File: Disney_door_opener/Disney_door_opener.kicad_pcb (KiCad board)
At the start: 2 copper layers, 70 x 43 mm, 29 parts, among them J1 Screw_Terminal_01x02, J2 Conn_01x02, J3 Conn_01x02, J4 Conn_01x05, J5 Screw_Terminal_01x02, U1 LM2596S-5, U2 ESP32_DevKit_V1_DOIT, U3 MAX98357A

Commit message: Changed esp32 board with 2 pinheader connectors. Updated resistor values for proper operation.
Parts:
- removed U2: ESP32_DevKit_V1_DOIT, Disney_door_opener:esp32_devkit_v1_doit
- added J6: Conn_01x15, Connector_PinHeader_2.54mm:PinHeader_1x15_P2.54mm_Vertical, F.Cu at (151.8, 32.5)
- added J7: Conn_01x15, Connector_PinHeader_2.54mm:PinHeader_1x15_P2.54mm_Vertical, F.Cu at (151.8, 58.0)
- R1, R2, R3, R5: value 100K -> DNI
- R4: value n.c. -> 630K
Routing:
- net Net-(J7-Pad8): vias 0 -> 1
- net Net-(J7-Pad7): vias 0 -> 1
- net GND: vias 238 -> 234

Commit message: Corrected swapped pins.
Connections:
- net Net-(J4-Pad3) renamed /CLK
- J4 pad 1: Net-(J4-Pad1) -> /LIGHT
- J4 pad 2: Net-(J4-Pad2) -> /CS
- J4 pad 4: Net-(J4-Pad4) -> /MISO
- J4 pad 5: Net-(J4-Pad5) -> /MOSI
- J6 pad 1: Net-(J4-Pad1) -> /MOSI
- J6 pad 10: Net-(J4-Pad4) -> Net-(J6-Pad10)
- J6 pad 6: Net-(J4-Pad2) -> /MISO
- J6 pad 8: Net-(J6-Pad8) -> /CS
- J7 pad 13: Net-(J4-Pad5) -> /LIGHT
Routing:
- net /MOSI: track 0.00 -> 57.6 mm, vias 0 -> 1
- net Net-(J4-Pad1): track 55.0 -> 0.00 mm
- net Net-(J4-Pad5): track 45.7 -> 0.00 mm
- net /MISO: track 0.00 -> 45.7 mm, vias 0 -> 2
- net Net-(J4-Pad2): track 40.3 -> 0.00 mm
- net /LIGHT: track 0.00 -> 34.7 mm
- net /CS: track 0.00 -> 32.8 mm
- net Net-(J4-Pad4): track 24.9 -> 0.00 mm
- net /CLK: track 37.2 -> 31.5 mm
- net GND: track 42.0 -> 46.7 mm, vias 234 -> 235
- net Net-(J7-Pad8): vias 1 -> 0
- net Net-(J7-Pad7): vias 1 -> 0
- net (no net): vias 3 -> 0

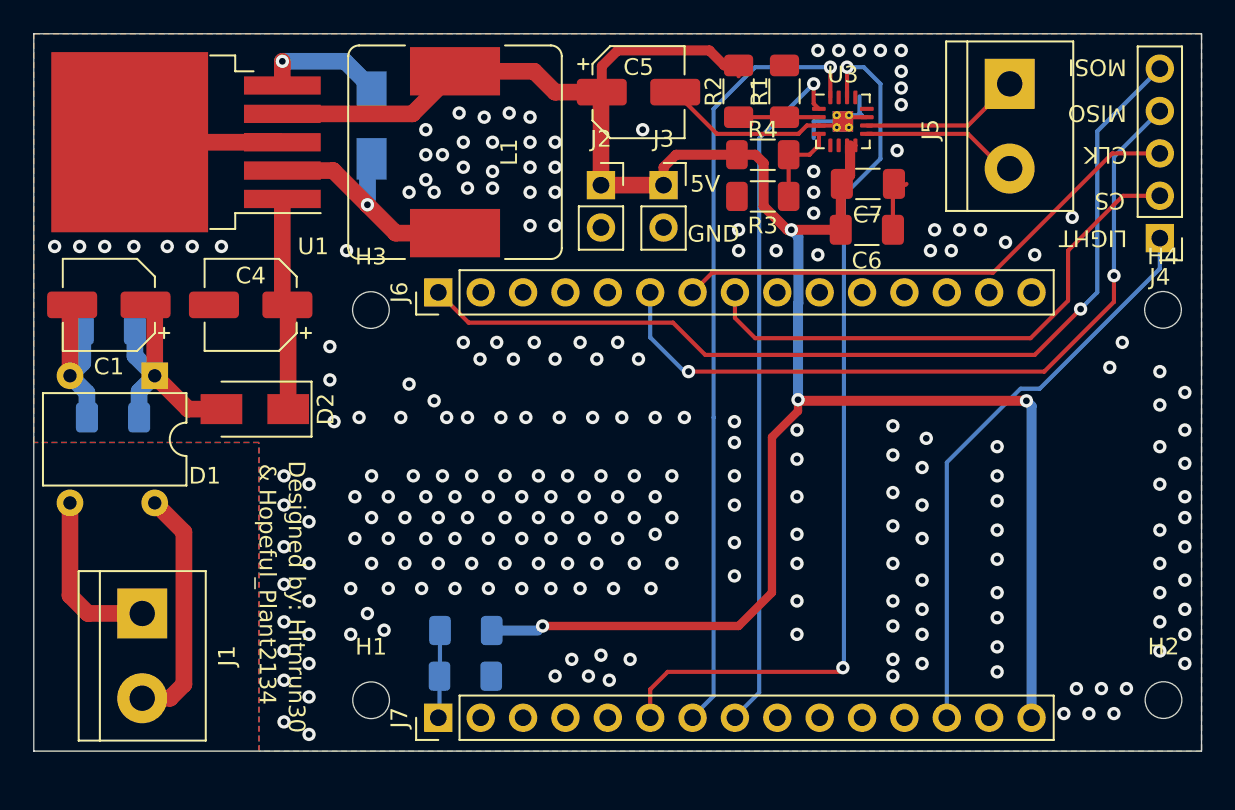
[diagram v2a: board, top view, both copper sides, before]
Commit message: Minor corrections. Changed pin headers to female.
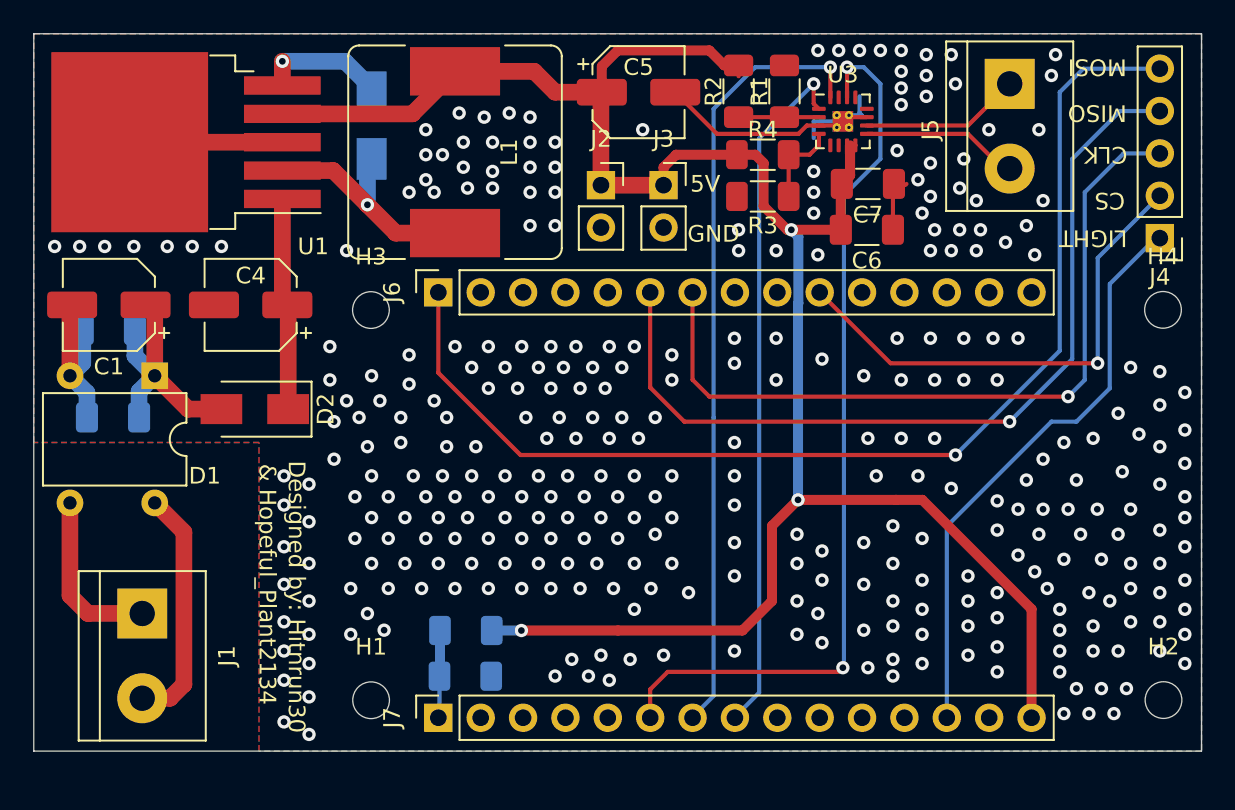
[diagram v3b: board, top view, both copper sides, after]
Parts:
- J6, J7: footprint Connector_PinHeader_2.54mm:PinHeader_1x15_P2.54mm_Vertical -> Connector_PinSocket_2.54mm:PinSocket_1x15_P2.54mm_Vertical
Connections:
- J6 pad 10: Net-(J6-Pad10) -> /CS
- J6 pad 8: /CS -> Net-(J6-Pad8)
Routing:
- net /CLK: track 31.5 -> 46.3 mm, vias 0 -> 1
- net /MOSI: track 57.6 -> 68.8 mm
- net +5V: track 138.5 -> 129.3 mm, vias 4 -> 3
- net /MISO: track 45.7 -> 51.8 mm, vias 2 -> 1
- net /CS: track 32.8 -> 30.0 mm, vias 0 -> 1
- net GND: vias 235 -> 329

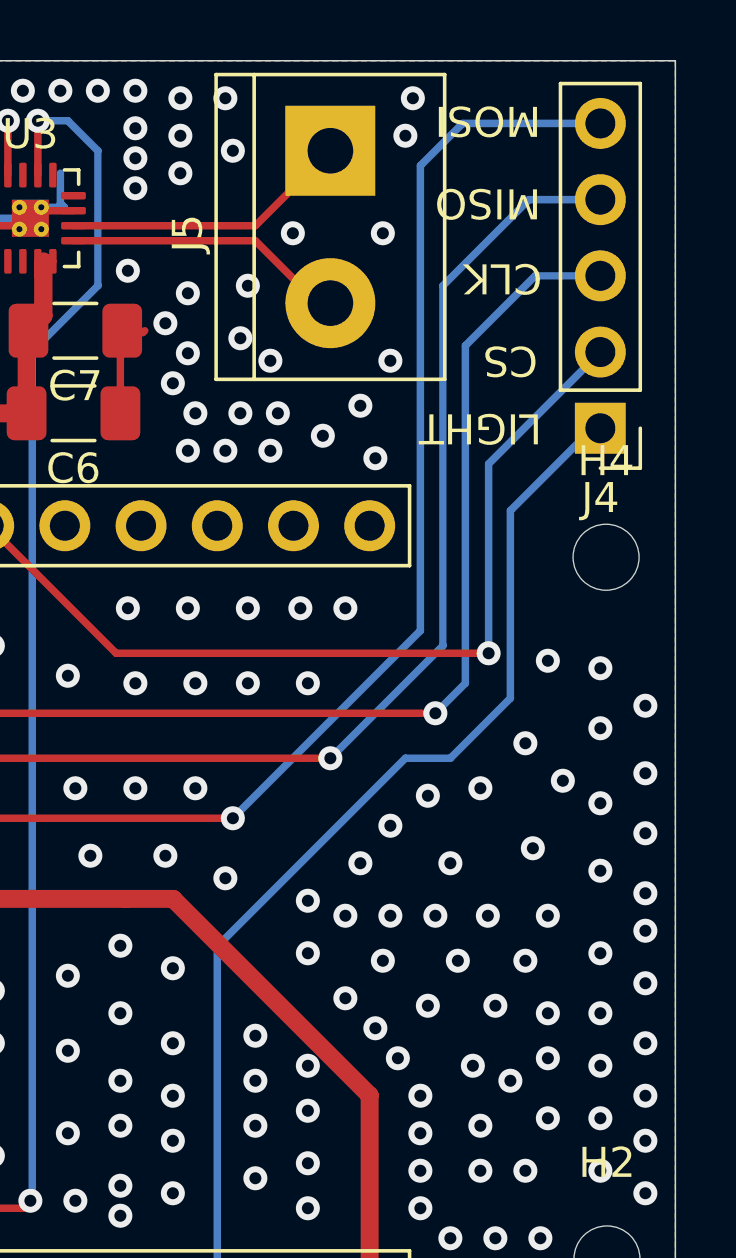
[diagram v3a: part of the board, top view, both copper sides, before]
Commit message: Removed one via and checked schematic and layout once more.
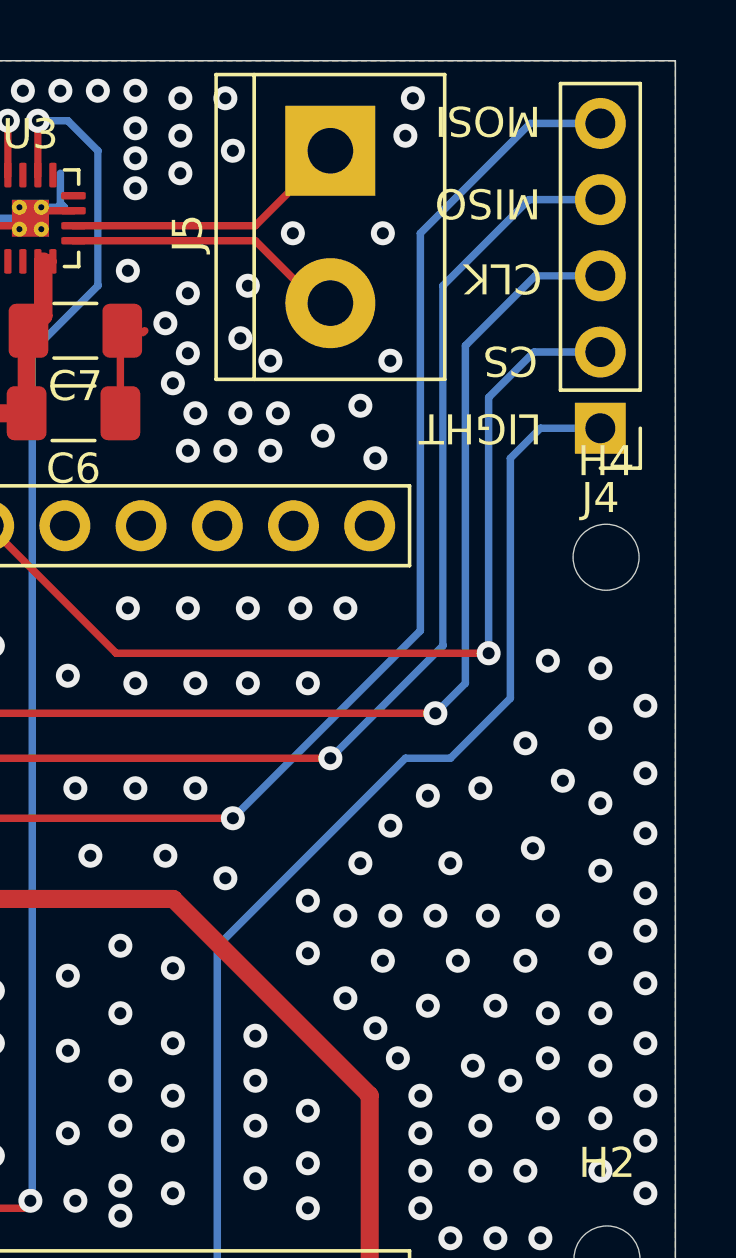
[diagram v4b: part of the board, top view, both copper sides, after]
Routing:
- net /MOSI: track 68.8 -> 67.5 mm
- net /CS: track 30.0 -> 31.3 mm
- net /LIGHT: track 35.1 -> 36.1 mm
- net GND: vias 329 -> 328
